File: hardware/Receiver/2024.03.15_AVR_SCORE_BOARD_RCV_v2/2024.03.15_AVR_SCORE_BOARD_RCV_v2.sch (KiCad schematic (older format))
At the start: 36 parts, among them J1 ARK_01x03, J3 UART, J4 Conn_01x03, J5 Conn_01x03, J6 Conn_01x03, U1 ATmega328P-PU, U2 AIMTEC_AMSROL-78NZ, U3 NRF24l04, U4 PCF8563T, Y1 16MHz, Y2 32,768kHz

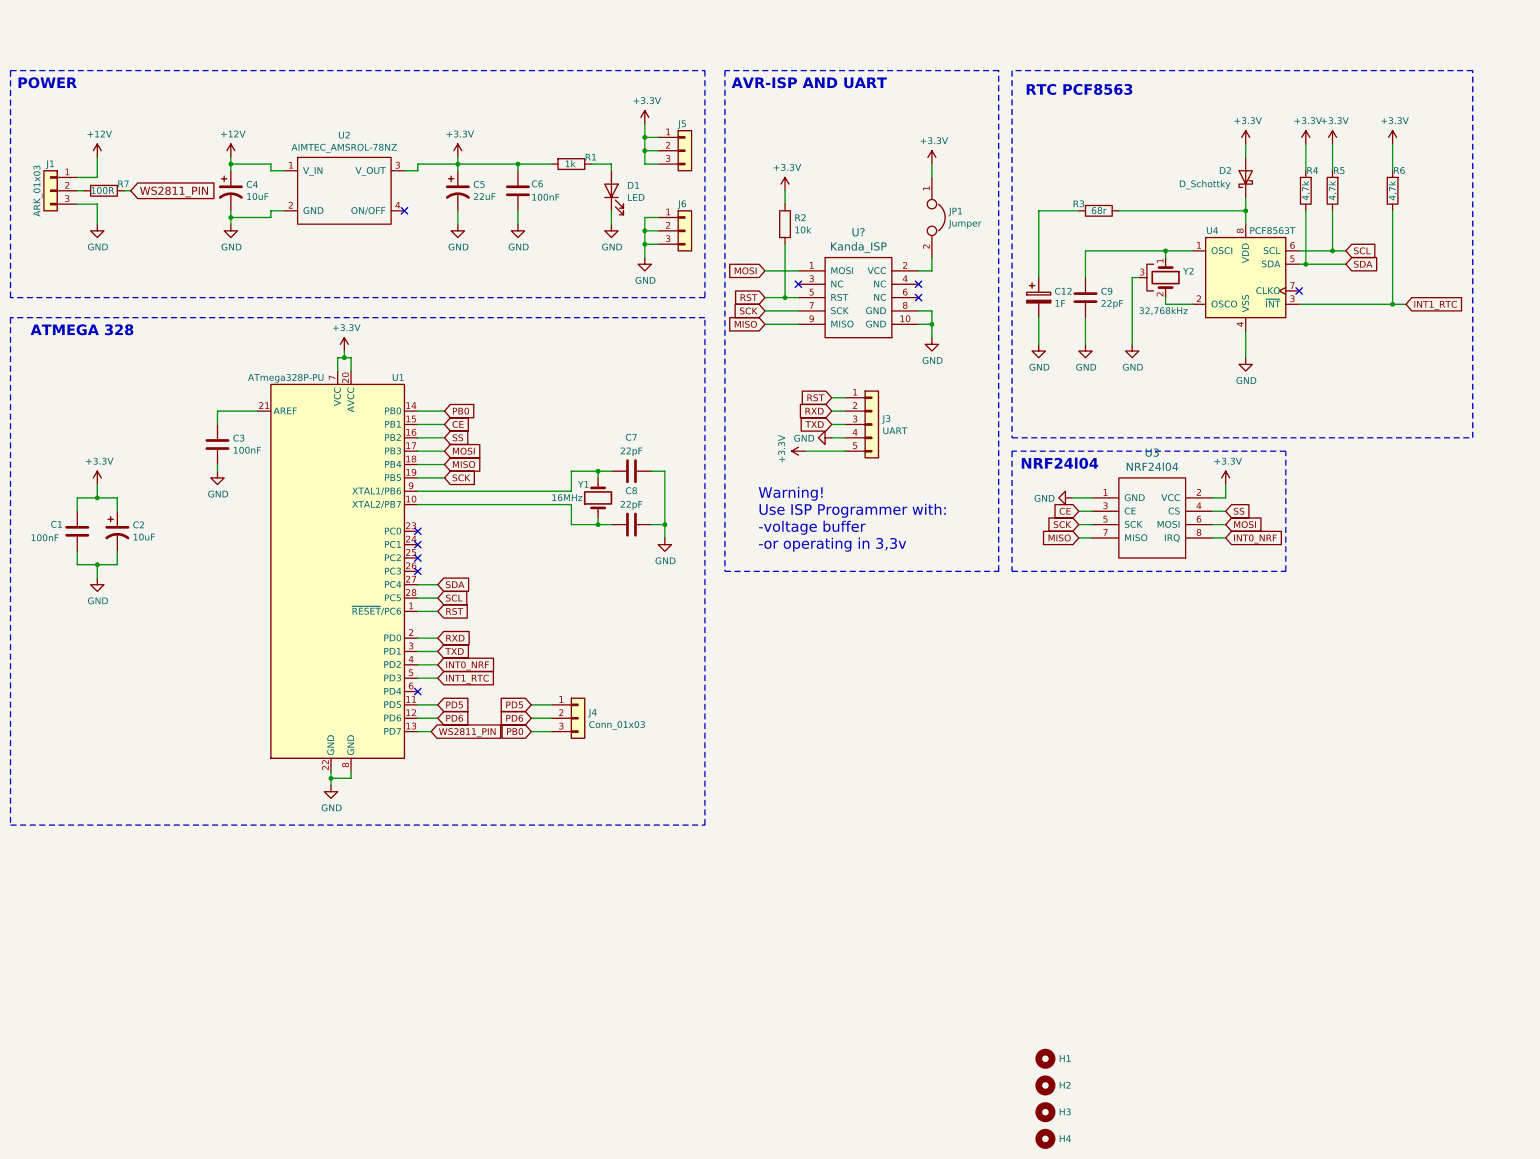
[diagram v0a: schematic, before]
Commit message: change design to 5v logic level
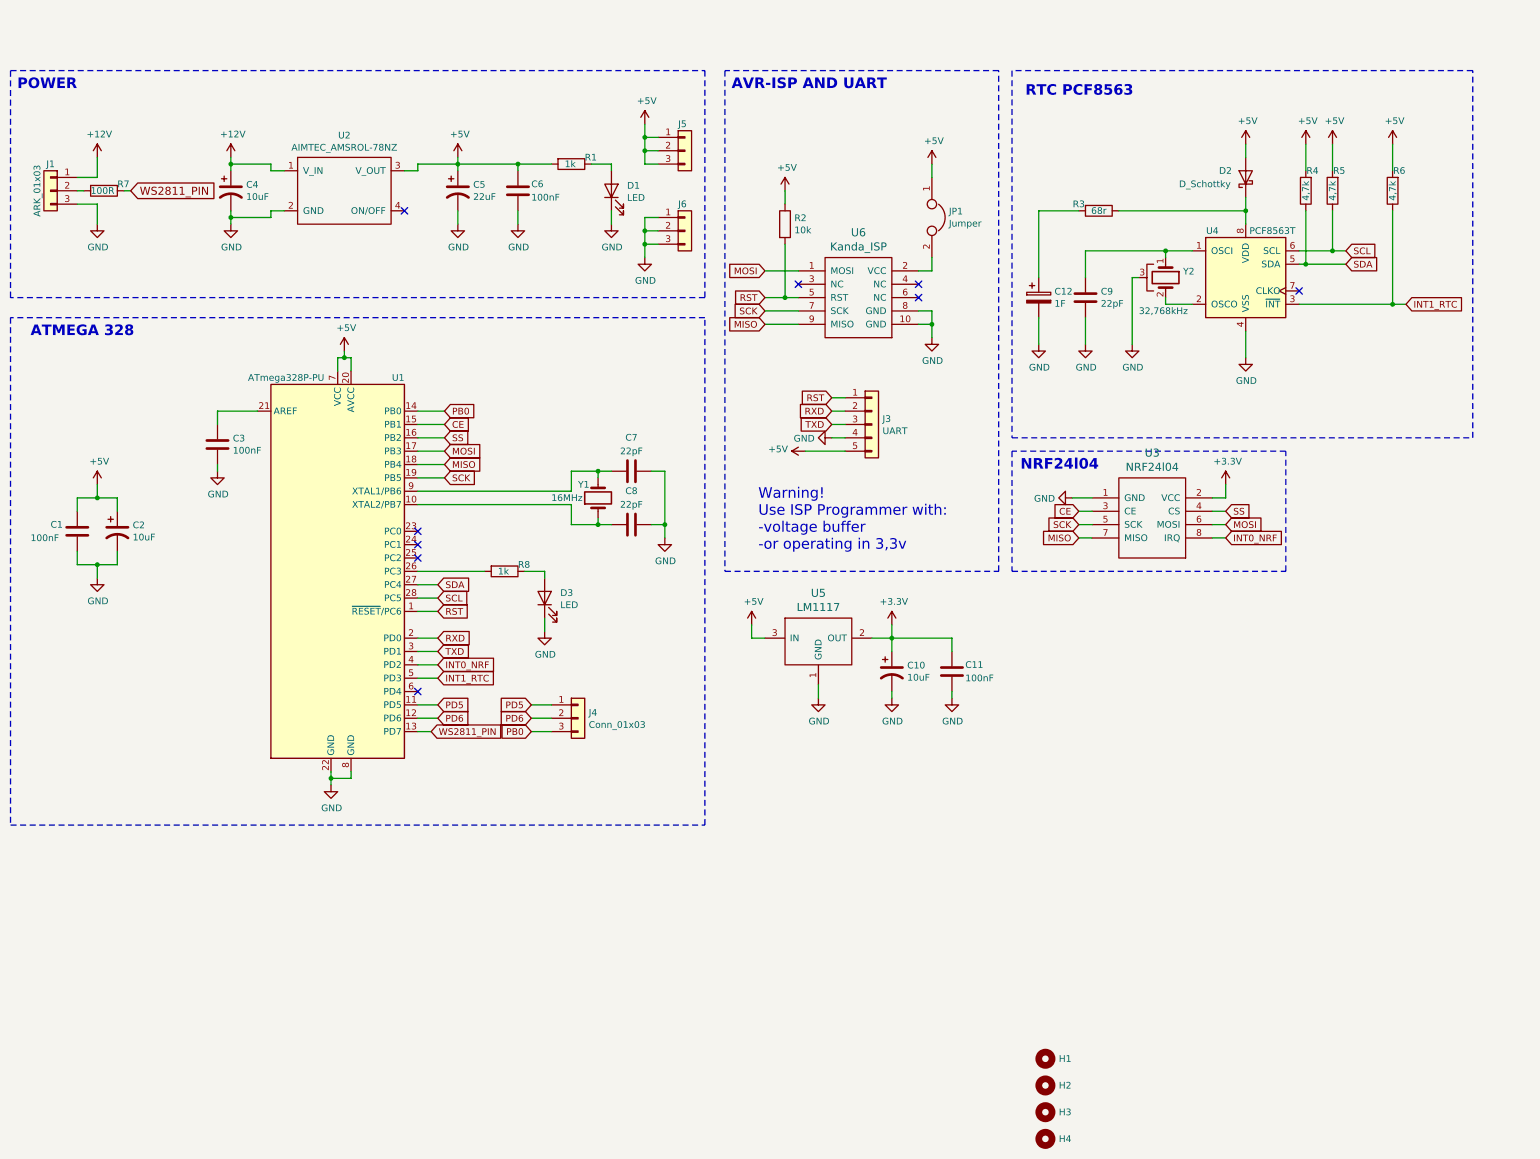
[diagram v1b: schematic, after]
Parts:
- added C10: 10uF, Moje:C(2,5mm), symbol Device:CP1
- added C11: 100nF, Moje:C[5,5mm], symbol Device:C
- added D3: LED, LED_THT:LED_D3.0mm, symbol Device:LED
- added R8: 1k, Moje:R_MY_DIN0204_L3.6mm_D1.6mm_P7.62mm, symbol Device:R
- added U5: LM1117, Moje:TO263_MY, symbol Moje:LM1117
- gave numbers to parts that had none: 1
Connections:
- net +3V3: now also C10.1, C11.1, U5.2 (OUT); no longer C1.1, C2.1, C5.1, C6.1, D2.2 (A), J3.5 (Pin_5), J5.1 (Pin_1), J5.2 (Pin_2), J5.3 (Pin_3), JP1.1, R1.2, R2.1, R4.2, R5.2, R6.2, U1.20 (AVCC), U1.7 (VCC), U2.3 (V_OUT)
- net GND: now also C10.2, C11.2, D3.1 (K), U5.1 (GND)
- net at U1.26 (PC3): now also R8.2
- new net: D3.2 (A), R8.1
- new net +5V: C1.1, C2.1, C5.1, C6.1, D2.2 (A), J3.5 (Pin_5), J5.1 (Pin_1), J5.2 (Pin_2), J5.3 (Pin_3), JP1.1, R1.2, R2.1, R4.2, R5.2, R6.2, U1.20 (AVCC), U1.7 (VCC), U2.3 (V_OUT), U5.3 (IN)
- no-connect marks 10 -> 9

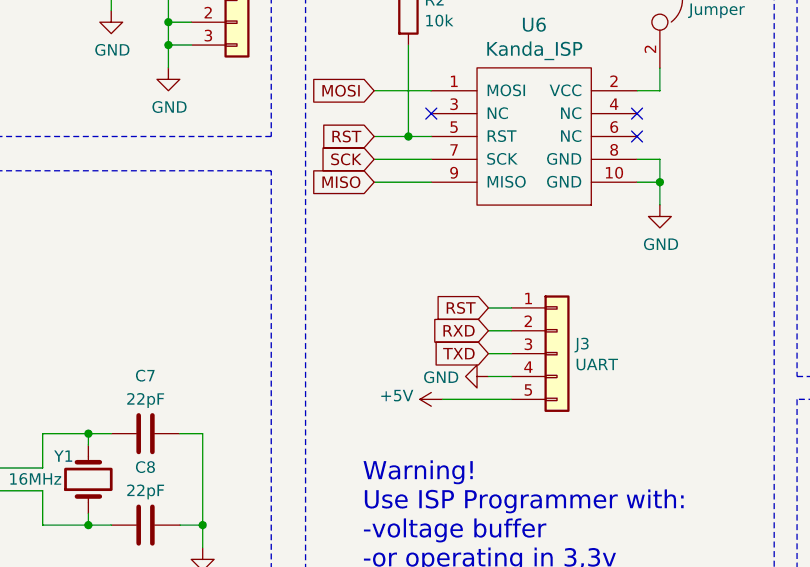
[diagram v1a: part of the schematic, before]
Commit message: changed wrong footprints
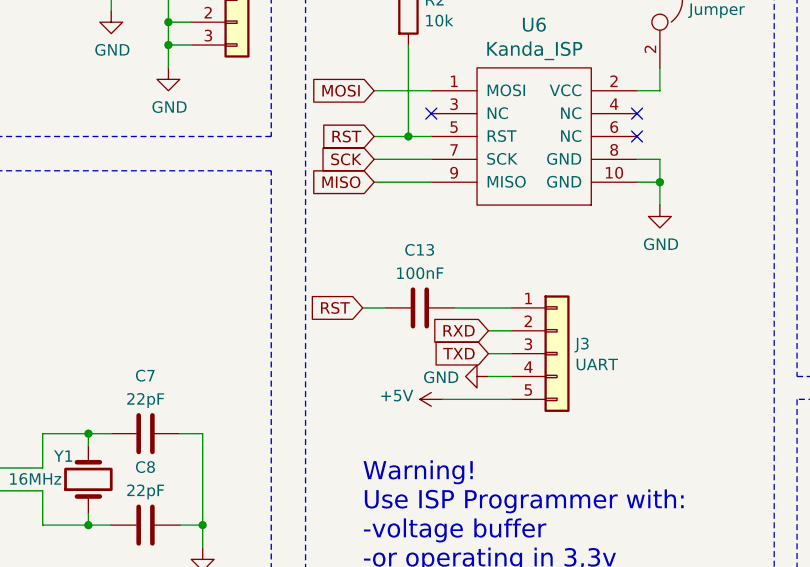
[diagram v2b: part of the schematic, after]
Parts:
- added C13: 100nF, Capacitor_SMD:C_0805_2012Metric_Pad1.15x1.40mm_HandSolder, symbol Device:C
- Y1: footprint Crystal:Crystal_HC52-6mm_Vertical -> Crystal:Crystal_HC49-U_Vertical
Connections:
- net RST: now also C13.2; no longer J3.1 (Pin_1)
- new net: C13.1, J3.1 (Pin_1)
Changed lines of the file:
@@
 F 0 "Y1" V 7550 5950 50  0000 R CNN
 F 1 "16MHz" V 7450 6150 50  0000 R CNN
-F 2 "Crystal:Crystal_HC52-6mm_Vertical" H 7450 5800 50  0001 C CNN
+F 2 "Crystal:Crystal_HC49-U_Vertical" H 7450 5800 50  0001 C CNN
 F 3 "~" H 7450 5800 50  0001 C CNN
 	1    7450 5800
@@
 Text GLabel 9200 5250 0    50   Input ~ 0
 TXD
-Text GLabel 9200 5050 0    50   Input ~ 0
+Text GLabel 8650 5050 0    50   Input ~ 0
 RST
 Wire Wire Line
@@
 	9300 5150 9200 5150
 Wire Wire Line
-	9300 5050 9200 5050
+	9300 5050 9050 5050
 $Comp
 L power:GND #PWR0127
@@
 Text GLabel 3950 3500 2    60   Input ~ 0
 WS2811_PIN
+$Comp
+L Device:C C13
+U 1 1 66698928
+P 8900 5050
+F 0 "C13" V 8648 5050 50  0000 C CNN
+F 1 "100nF" V 8750 5050 50  0000 C CNN
+F 2 "Capacitor_SMD:C_0805_2012Metric_Pad1.15x1.40mm_HandSolder" H 8938 4900 50  0001 C CNN
+F 3 "~" H 8900 5050 50  0001 C CNN
+	1    8900 5050
+	0    1    1    0
+$EndComp
+Wire Wire Line
+	8650 5050 8750 5050
 $EndSCHEMATC

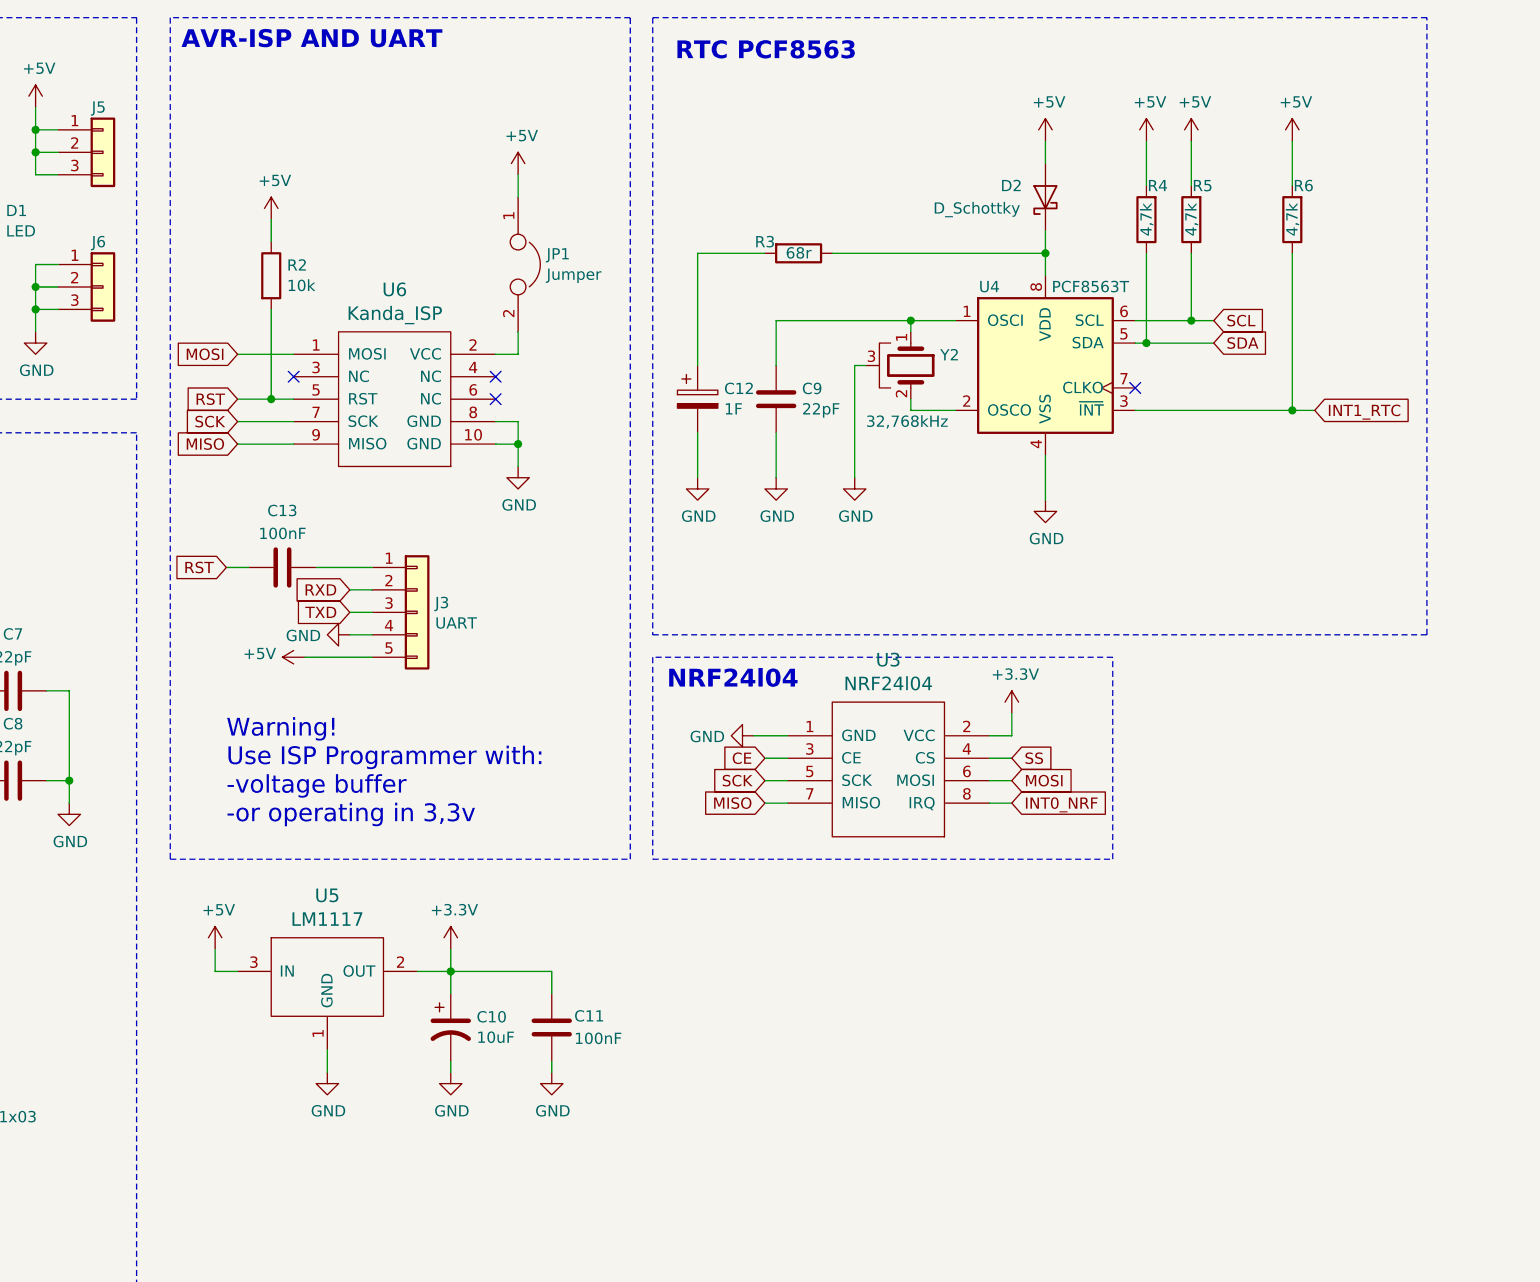
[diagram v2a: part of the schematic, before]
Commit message: Added 100nF capacitor for rtc
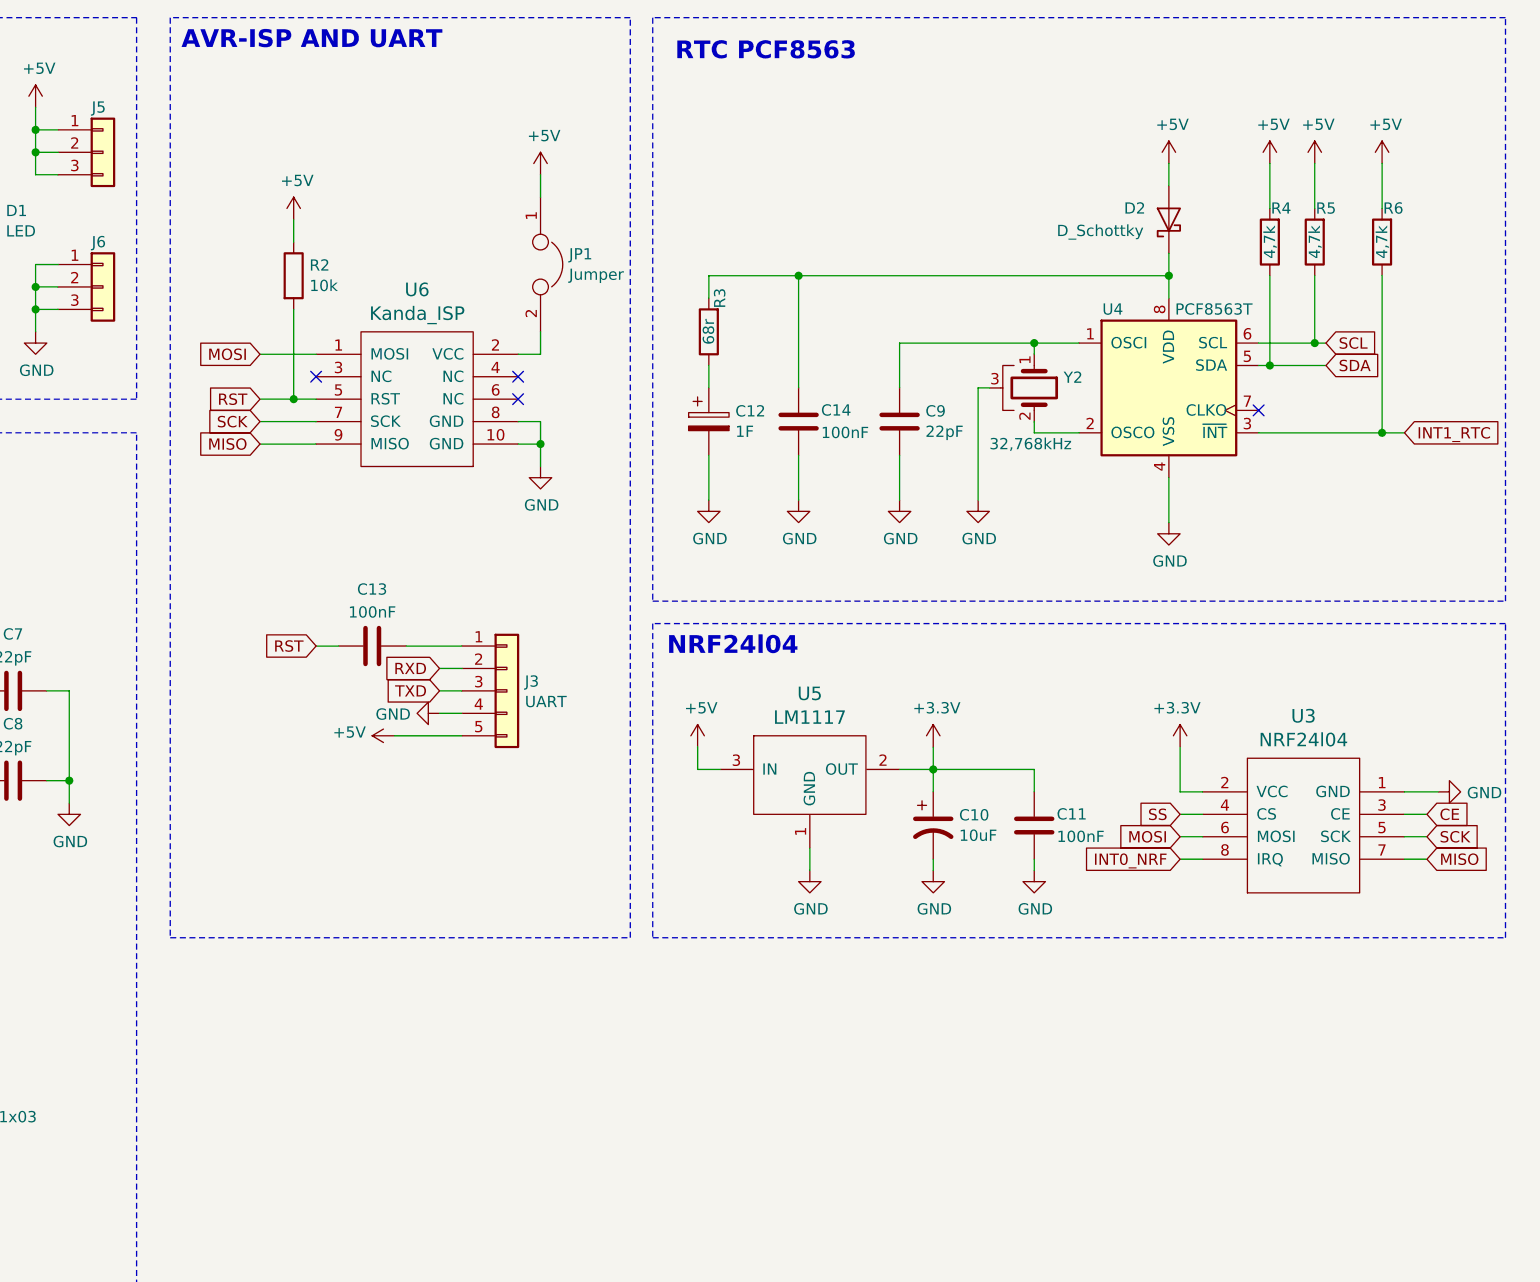
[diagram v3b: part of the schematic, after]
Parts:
- added C14: 100nF, Moje:C[5,5mm], symbol Device:C
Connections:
- net GND: now also C14.2
- net at C12.1: now also R3.1; no longer R3.2
- net at D2.1 (K), U4.8 (VDD): now also R3.2, C14.1; no longer R3.1
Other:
- note removed: "Warning!\nUse ISP Programmer with:\n-voltage buffer\n-or operating in 3,3v"
- moved on the sheet: C10, C11, C12, C13, C9, D2, J3, JP1, R2, R3, R4, R5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

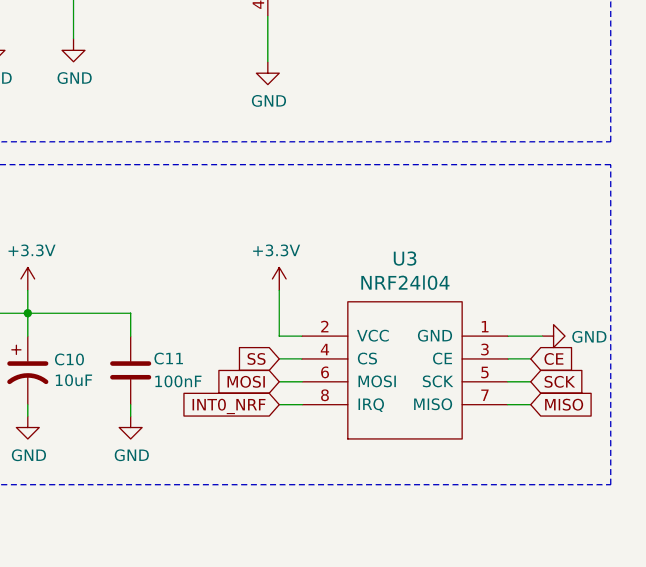
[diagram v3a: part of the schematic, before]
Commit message: Fixed NRF24L01 schematic symbol
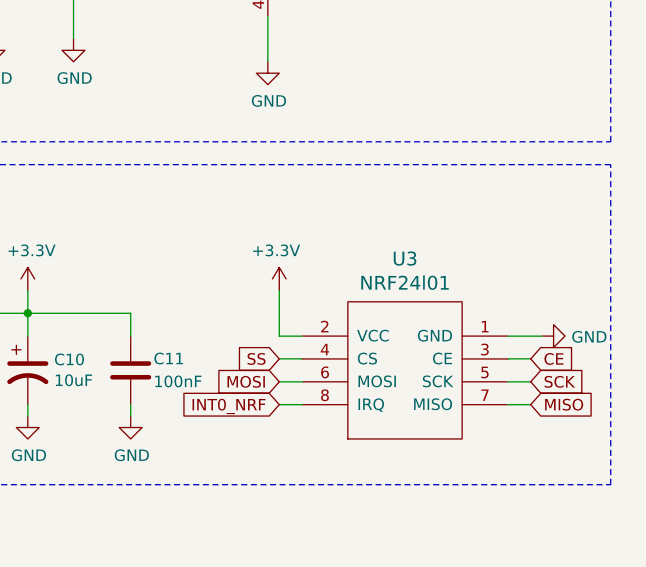
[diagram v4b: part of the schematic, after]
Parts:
- removed U3: NRF24l04, Moje:NRF24l01, symbol Moje:NRF24l04
- added U3: NRF24l01, Moje:NRF24l01, symbol Moje:NRF24l01
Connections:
- net +3V3: now also U3.2 (VCC)
- net CE: now also U3.3 (CE)
- net GND: now also U3.1 (GND)
- net INT0_NRF: now also U3.8 (IRQ)
- net MISO: now also U3.7 (MISO)
- net MOSI: now also U3.6 (MOSI)
- net SCK: now also U3.5 (SCK)
- net SS: now also U3.4 (CS)
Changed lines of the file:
@@
 	12900 6050 13000 6050
-$Comp
-L Moje:NRF24l04 U3
-U 1 1 65F55076
-P 13450 6200
-F 0 "U3" H 13450 5713 60  0000 C CNN
-F 1 "NRF24l04" H 13450 5819 60  0000 C CNN
-F 2 "Moje:NRF24l01" H 13450 6550 60  0001 C CNN
-F 3 "" H 13450 6550 60  0001 C CNN
-	1    13450 6200
-	1    0    0    1
-$EndComp
 $Comp
 L power:GND #PWR0101
@@
 	-1   0    0    -1
 $EndComp
+$Comp
+L Moje:NRF24l01 U3
+U 1 1 663D77C2
+P 13450 6200
+F 0 "U3" H 13450 5713 60  0000 C CNN
+F 1 "NRF24l01" H 13450 5819 60  0000 C CNN
+F 2 "Moje:NRF24l01" H 13450 6550 60  0001 C CNN
+F 3 "" H 13450 6550 60  0001 C CNN
+	1    13450 6200
+	1    0    0    1
+$EndComp
 $EndSCHEMATC
